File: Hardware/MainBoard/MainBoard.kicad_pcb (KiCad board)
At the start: 2 copper layers, 100 x 90 mm, 20 parts, among them J5 USB_B_Micro, U3 LD1117ASTR

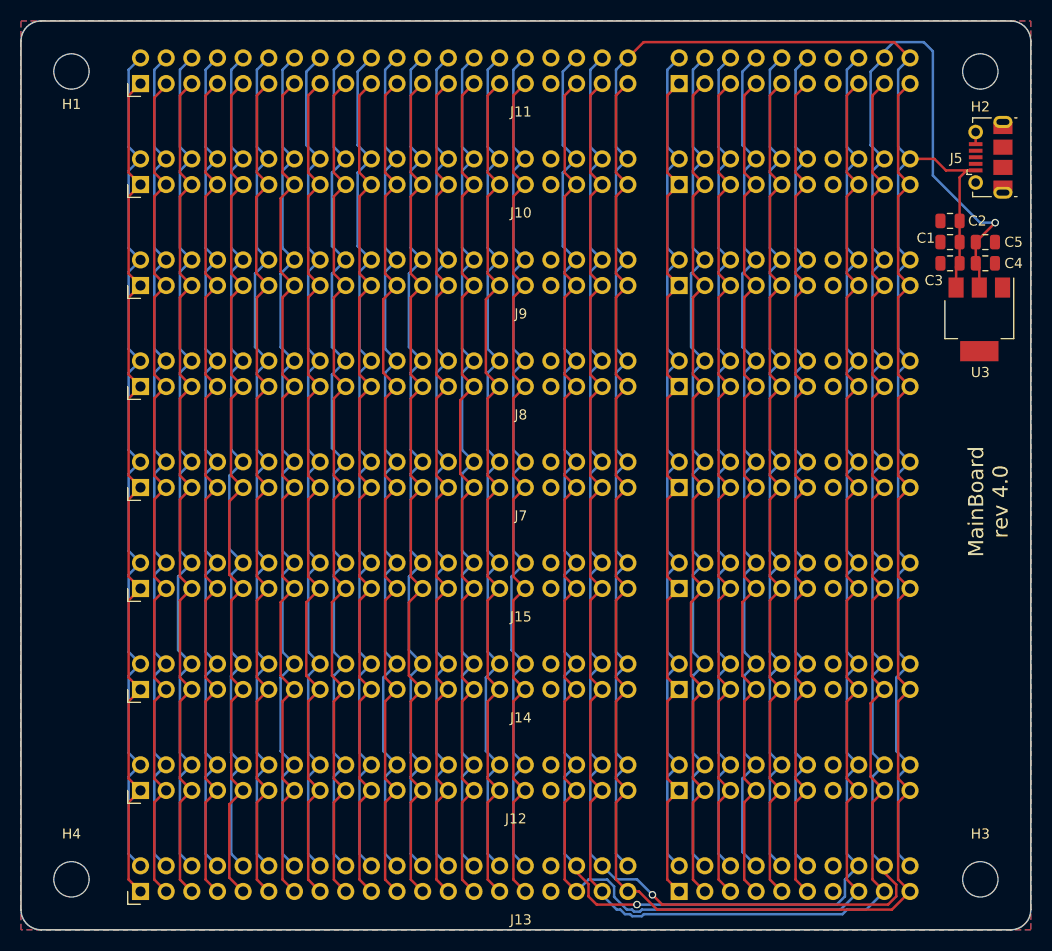
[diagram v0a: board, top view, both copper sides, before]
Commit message: rework CI, make PCB smaller
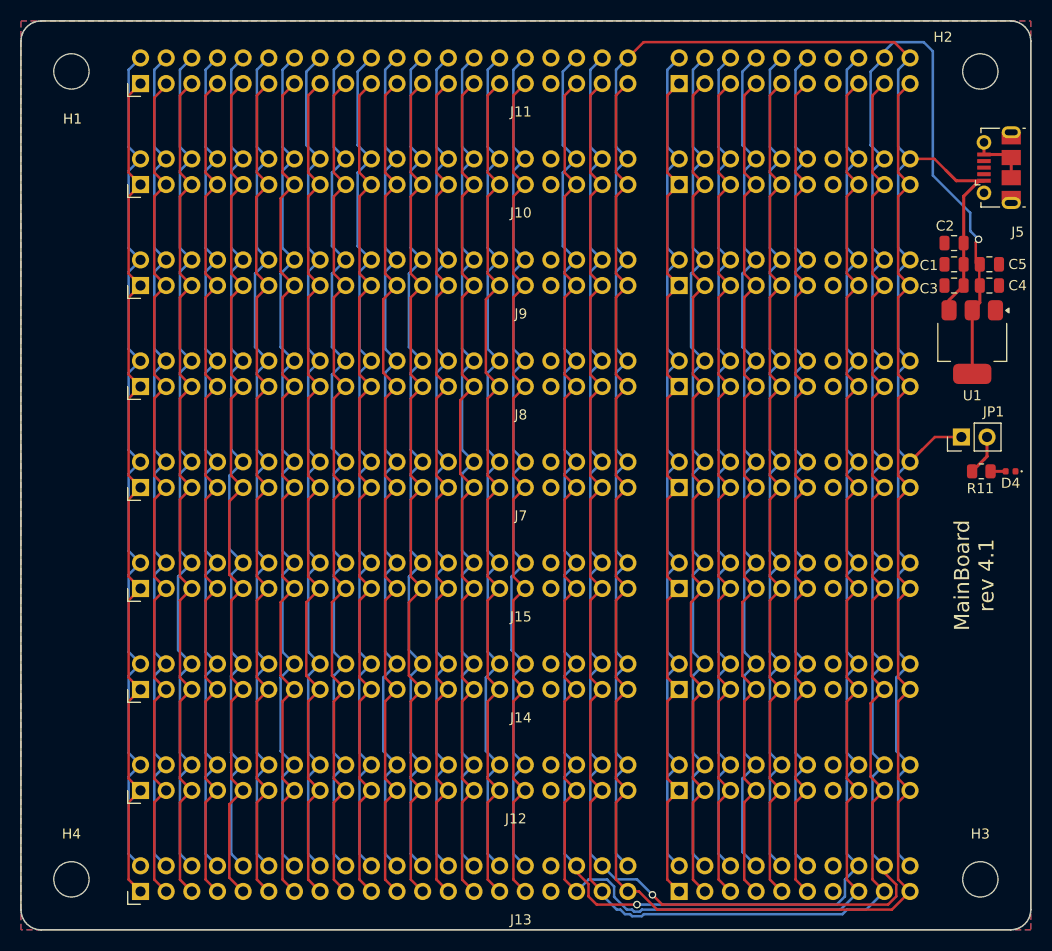
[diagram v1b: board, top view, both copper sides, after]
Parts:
- removed U3: LD1117ASTR, Package_TO_SOT_SMD:SOT-223
- added D4: LED, LED_SMD:LED_0402_1005Metric, F.Cu at (153.0, 71.6)
- added JP1: Jumper_2_Open, Connector_PinHeader_2.54mm:PinHeader_1x02_P2.54mm_Vertical, F.Cu at (148.1, 68.2)
- added R11: 1k, Resistor_SMD:R_0805_2012Metric, F.Cu at (150.1, 71.6)
- added U1: LD1117S50TR_SOT223, Package_TO_SOT_SMD:SOT-223-3_TabPin2, F.Cu at (149.2, 58.8)
- J5: footprint Connector_USB:USB_Micro-B_Molex-105017-0001 -> HardwareDataLogger:USB_Micro-B_Molex-105017-0001_Extra_Mechanical_Pads
- moved C1 2.24 mm to (147.4, 51.1)
- moved C2 2.24 mm to (147.4, 49.0)
- moved C3 2.24 mm to (147.4, 53.2)
- moved C4 2.24 mm to (150.9, 53.2)
- moved C5 2.24 mm to (150.9, 51.1)
- moved J5 2.03 mm to (149.6, 41.9)
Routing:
- net 5V: track 224.4 -> 235.6 mm
- net 3V3_FROM_MAINBOARD: track 242.4 -> 249.3 mm
- net GND: track 89.0 -> 93.5 mm
- net Net-(JP1-B): track 0.00 -> 4.01 mm
- net Net-(D4-A): track 0.00 -> 1.50 mm
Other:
- board text added: "MainBoard rev 4.1"
- board text removed: "MainBoard rev 4.0"
